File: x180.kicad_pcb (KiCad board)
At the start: 6 copper layers, 50 x 50 mm, 74 parts, among them J1 U180 Header, J2 Conn_01x06_Pin, U1 ATF1502AS-7A, U2 ADG734, U3 ADG734, U4 ADG734, U5 ADG734

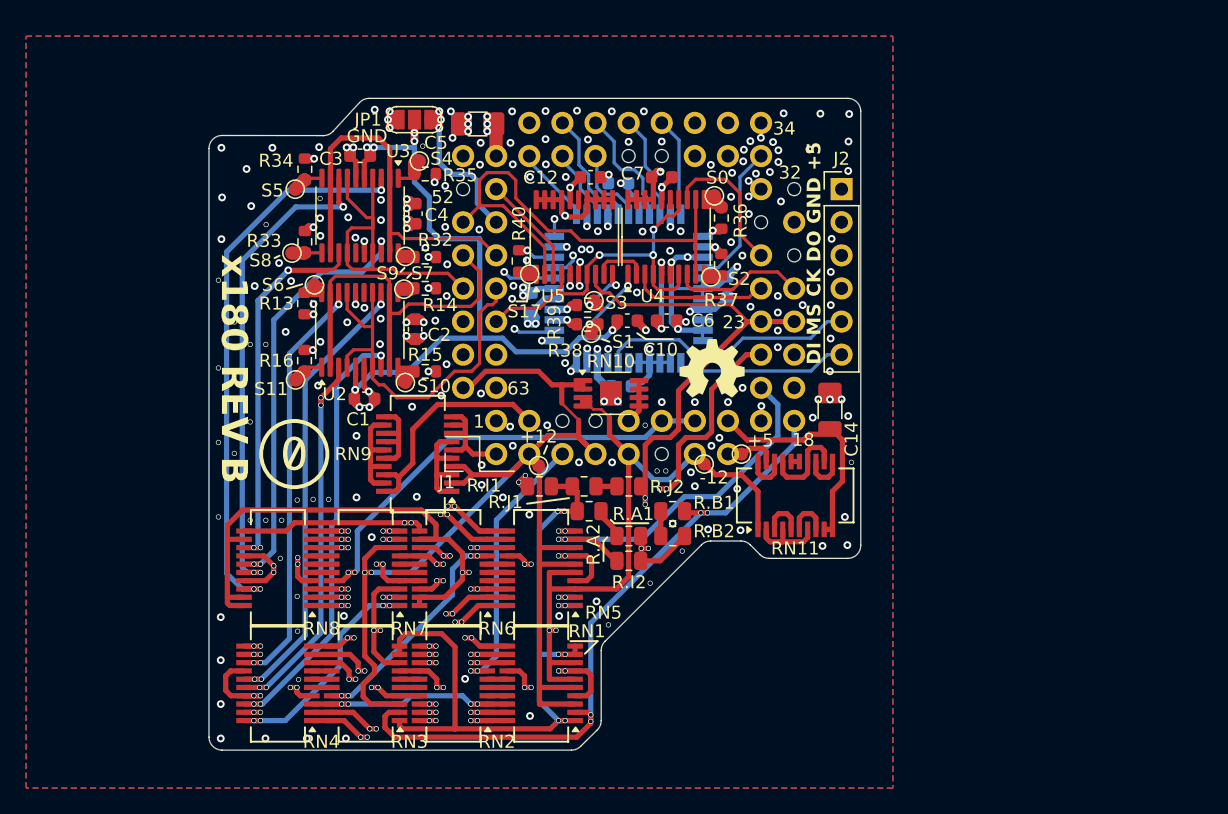
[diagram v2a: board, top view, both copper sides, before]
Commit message: REV C: optimized for low stray capacitance & back to discrete resistors
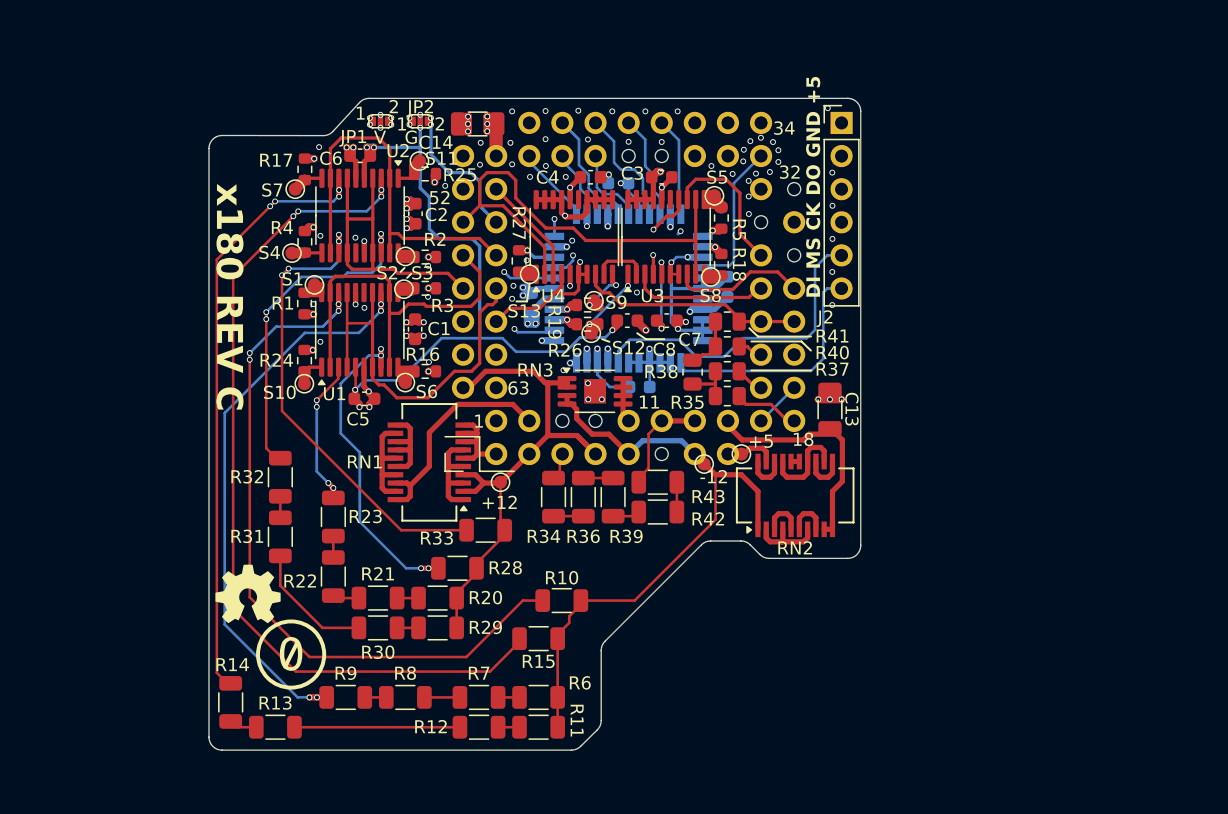
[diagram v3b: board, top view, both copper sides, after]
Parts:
- removed R.A1, R.A2, R.B1, R.B2, R.J1, R.J2: 300k, Resistor_SMD:R_0805_2012Metric
- removed R.I1, R.I2: 100k, Resistor_SMD:R_0805_2012Metric
- removed the RN1 at (72.3, 89.3)
- removed the RN2 at (65.6, 89.3)
- removed the RN3 at (58.9, 89.3)
- removed RN4, RN5, RN6, RN7, RN8: OSOP 20k, MiDi:SSOP-20_3.9x8.7mm_P0.635mm
- added JP1: SolderJumper_3_Open, MiDi:SolderJumper-3_P0.7mm_Open_RoundedPad0.7x0.4mm, F.Cu at (60.0, 46.2)
- added R10: 20k, Resistor_SMD:R_1206_3216Metric, F.Cu at (73.9, 83.0)
- added R11: 20k, Resistor_SMD:R_1206_3216Metric, F.Cu at (72.1, 92.7)
- added R12: 20k, Resistor_SMD:R_1206_3216Metric, F.Cu at (67.6, 92.7)
- added R13: 20k, Resistor_SMD:R_1206_3216Metric, F.Cu at (51.9, 92.7)
- added R14: 20k, Resistor_SMD:R_1206_3216Metric, F.Cu at (48.5, 90.8)
- added R15: 20k, Resistor_SMD:R_1206_3216Metric, F.Cu at (72.1, 85.9)
- added R20: 20k, Resistor_SMD:R_1206_3216Metric, F.Cu at (64.4, 82.8)
- added R21: 20k, Resistor_SMD:R_1206_3216Metric, F.Cu at (59.8, 82.8)
- added R22: 20k, Resistor_SMD:R_1206_3216Metric, F.Cu at (56.4, 81.2)
- added R23: 20k, Resistor_SMD:R_1206_3216Metric, F.Cu at (56.4, 76.6)
- added R28: 20k, Resistor_SMD:R_1206_3216Metric, F.Cu at (65.9, 80.5)
- added R29: 20k, Resistor_SMD:R_1206_3216Metric, F.Cu at (64.4, 85.1)
- added R30: 20k, Resistor_SMD:R_1206_3216Metric, F.Cu at (59.8, 85.1)
- added R31: 20k, Resistor_SMD:R_1206_3216Metric, F.Cu at (52.3, 78.1)
- added R32: 20k, Resistor_SMD:R_1206_3216Metric, F.Cu at (52.3, 73.5)
- added R33: 20k, Resistor_SMD:R_1206_3216Metric, F.Cu at (68.1, 77.6)
- added R34: 10k, Resistor_SMD:R_1206_3216Metric, F.Cu at (73.3, 75.1)
- added R35: 37k5, Resistor_SMD:R_0805_2012Metric, F.Cu at (86.6, 67.3)
- added R36: 10k, Resistor_SMD:R_1206_3216Metric, F.Cu at (75.6, 75.1)
- added R37: 16k7, Resistor_SMD:R_0805_2012Metric, F.Cu at (86.6, 65.4)
- added R38: 37k5, Resistor_SMD:R_0805_2012Metric, F.Cu at (83.9, 65.5)
- added R39: 10k, Resistor_SMD:R_1206_3216Metric, F.Cu at (77.9, 75.1)
- added R40: 16k7, Resistor_SMD:R_0805_2012Metric, F.Cu at (86.6, 63.5)
- added R41: 37k5, Resistor_SMD:R_0805_2012Metric, F.Cu at (86.6, 61.6)
- added R42: 10k, Resistor_SMD:R_1206_3216Metric, F.Cu at (81.3, 76.2)
- added R43: 10k, Resistor_SMD:R_1206_3216Metric, F.Cu at (81.3, 73.9)
- added R6: 20k, Resistor_SMD:R_1206_3216Metric, F.Cu at (72.1, 90.4)
- added R7: 20k, Resistor_SMD:R_1206_3216Metric, F.Cu at (67.6, 90.4)
- added R8: 20k, Resistor_SMD:R_1206_3216Metric, F.Cu at (61.9, 90.4)
- added R9: 20k, Resistor_SMD:R_1206_3216Metric, F.Cu at (57.3, 90.4)
- JP2: renamed from JP1; footprint Jumper:SolderJumper-3_P1.3mm_Open_RoundedPad1.0x1.5mm -> MiDi:SolderJumper-3_P0.7mm_Open_RoundedPad0.7x0.4mm
- moved G*** 39.6 mm to (49.8, 82.5)
- moved REF** 21.2 mm to (51.4, 76.0)
- moved REF** 18.0 mm to (51.6, 67.8)
- moved REF** 16.2 mm to (63.5, 87.2)
- moved J2 5.08 mm to (95.4, 46.4)
- moved +12 3.19 mm to (69.2, 73.9)
- moved C11 1.40 mm to (79.9, 66.6)
- moved RN3 1.23 mm to (76.5, 66.9)
- moved RN1 1.09 mm to (63.8, 72.4)
- moved S10 0.73 mm to (54.2, 66.4)
- moved JP2 0.46 mm to (63.1, 46.2)
- renumbered C2 to C1, C9 to C10, C13 to C12, C14 to C13, C5 to C14, C4 to C2, C7 to C3, C12 to C4, C1 to C5, C3 to C6, C6 to C7, C10 to C8, C8 to C9, R13 to R1, R15 to R16, R34 to R17, R37 to R18, R39 to R19, R32 to R2, R16 to R24, R35 to R25, R38 to R26, R40 to R27, R14 to R3, R33 to R4, R36 to R5, RN9 to RN1, RN11 to RN2, RN10 to RN3, S6 to S1, S11 to S10, S4 to S11, S1 to S12, S17 to S13, S9 to S2, S7 to S3, S8 to S4, S0 to S5, S10 to S6, S5 to S7, S2 to S8, S3 to S9, U2 to U1, U3 to U2, U4 to U3, U5 to U4, U1 to U5
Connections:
- C1 pad 1: GND -> GND1
- C10 pad 1: VDD -> VDD1
- C10 pad 2: GND -> GND1
- C11 pad 1: VDD -> VDD1
- C11 pad 2: GND -> GND1
- C12 pad 1: VDD -> VDD1
- C12 pad 2: GND -> GND1
- C14 pad 1: GND -> GND1
- C14 pad 2: VDD -> VDD1
- C2 pad 1: GND -> GND1
- C3 pad 1: GND -> GND1
- C4 pad 1: GND -> GND1
- C5 pad 2: GND -> GND1
- C6 pad 2: GND -> GND1
- C7 pad 2: GND -> GND1
- C8 pad 2: GND -> GND1
- C9 pad 1: VDD -> VDD1
- C9 pad 2: GND -> GND1
- J1 pad 1: GND -> GND1
- J1 pad 17: GND -> GND1
- J1 pad 20: GND -> GND1
- J1 pad 22: GND -> GND1
- J1 pad 30: GND -> GND1
- J1 pad 31: GND -> GND1
- J1 pad 34: GND -> GND1
- J1 pad 35: GND -> GND1
- J1 pad 36: GND -> GND1
- J1 pad 37: GND -> GND1
- J1 pad 38: GND -> GND1
- J1 pad 48: GND -> GND1
- J1 pad 49: VDD -> VDD1
- J1 pad 50: GND -> GND1
- J1 pad 59: GND -> GND1
- J1 pad 60: GND -> GND1
- J1 pad 61: GND -> GND1
- J1 pad 62: GND -> GND1
- J1 pad 63: GND -> GND1
- J2 pad 1: VDD -> VDD1
- J2 pad 2: GND -> GND1
- JP2 pad 3: GND -> GND1
- RN3 pad 9: GND -> PIN3 +12_GND
- U1 pad 6: GND -> GND1
- U2 pad 6: GND -> GND1
- U3 pad 14: GND -> GND1
- U3 pad 17: GND -> GND1
- U3 pad 18: GND -> GND1
- U3 pad 19: GND -> GND1
- U3 pad 20: GND -> GND1
- U3 pad 4: GND -> GND1
- U3 pad 6: GND -> GND1
- U3 pad 7: GND -> GND1
- U4 pad 11: GND -> GND1
- U4 pad 12: GND -> GND1
- U4 pad 13: GND -> GND1
- U4 pad 14: GND -> GND1
- U4 pad 17: GND -> GND1
- U4 pad 18: GND -> GND1
- U4 pad 19: GND -> GND1
- U4 pad 20: GND -> GND1
- U4 pad 4: GND -> GND1
- U4 pad 6: GND -> GND1
- U4 pad 7: GND -> GND1
- U5 pad 16: GND -> GND1
- U5 pad 17: VDD -> VDD1
- U5 pad 2: GND -> GND1
- U5 pad 24: GND -> GND1
- U5 pad 29: VDD -> VDD1
- U5 pad 3: GND -> GND1
- U5 pad 36: GND -> GND1
- U5 pad 38: GND -> GND1
- U5 pad 39: GND -> GND1
- U5 pad 4: GND -> GND1
- U5 pad 40: GND -> GND1
- U5 pad 41: VDD -> VDD1
- U5 pad 42: GND -> GND1
- U5 pad 43: GND -> GND1
- U5 pad 44: GND -> GND1
- U5 pad 5: GND -> GND1
- U5 pad 6: GND -> GND1
- U5 pad 8: GND -> GND1
- U5 pad 9: VDD -> VDD1
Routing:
- net GND1: track 0.00 -> 408.1 mm, vias 0 -> 83
- net GND: track 97.3 -> 0.00 mm, vias 207 -> 0
- net PIN21 LADT1: track 72.0 -> 1.94 mm, vias 8 -> 0
- net Net-(RN6A-R1.2): track 61.7 -> 0.00 mm, vias 4 -> 0
- net Net-(RN1A-R1.1): track 54.5 -> 0.00 mm, vias 6 -> 0
- net (no net): track 0.00 -> 53.9 mm
- net +12_REF: track 96.7 -> 43.1 mm, vias 2 -> 0
- net VDD1: track 0.00 -> 52.2 mm, vias 0 -> 10
- net PIN23 LAD: track 69.1 -> 17.2 mm, vias 4 -> 0
- net Net-(RN2A-R1.2): track 49.5 -> 0.00 mm, vias 8 -> 0
- net PIN18 LADEXT: track 53.0 -> 5.08 mm, vias 4 -> 0
- net Net-(RN2B-R2.2): track 45.8 -> 0.00 mm, vias 8 -> 0
- net Net-(RN2J-R10.2): track 45.2 -> 0.00 mm, vias 8 -> 0
- net Net-(RN3D-R4.2): track 45.1 -> 0.00 mm, vias 8 -> 0
- net PIN19 LADT2: track 45.2 -> 2.20 mm, vias 4 -> 0
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- added copper zone on In4.Cu, net GND1
- added copper zone on In1.Cu, net PIN3 +12_GND
- added copper zone on In2.Cu, net VDD1
- removed copper zone on B.Cu, net GND
- removed copper zone on F.Cu, net GND
- removed copper zone on In1.Cu, net GND
- removed copper zone on In2.Cu, net GND
- removed copper zone on In3.Cu, net GND
- removed copper zone on In4.Cu, net GND
- removed copper zone on In2.Cu, net VDD
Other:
- rule pad_to_mask_clearance: 0.0508 -> 0
- board text added: "11"
- board text added: "2"
- board text added: "G"
- board text added: "Michael D. 11/2025"
- board text added: "V"
- board text added: "x180 REV C"
- board text removed: "23"
- board text removed: "GND"
- board text removed: "Michael D. 10/2025"
- board text removed: "x180 REV B"
